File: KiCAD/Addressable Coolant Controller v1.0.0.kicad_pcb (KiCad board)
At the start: 2 copper layers, 117.2 x 159.5 mm, 56 parts, among them J1 XW4M-10D2-H1DS, J2 XW4M-02D1-H1DA, K1 G5V-1, K2 G5V-1, K3 G5V-1, K4 G5V-1, K5 G5V-1, K6 G5V-1, K7 G5V-1, K8 G5V-1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

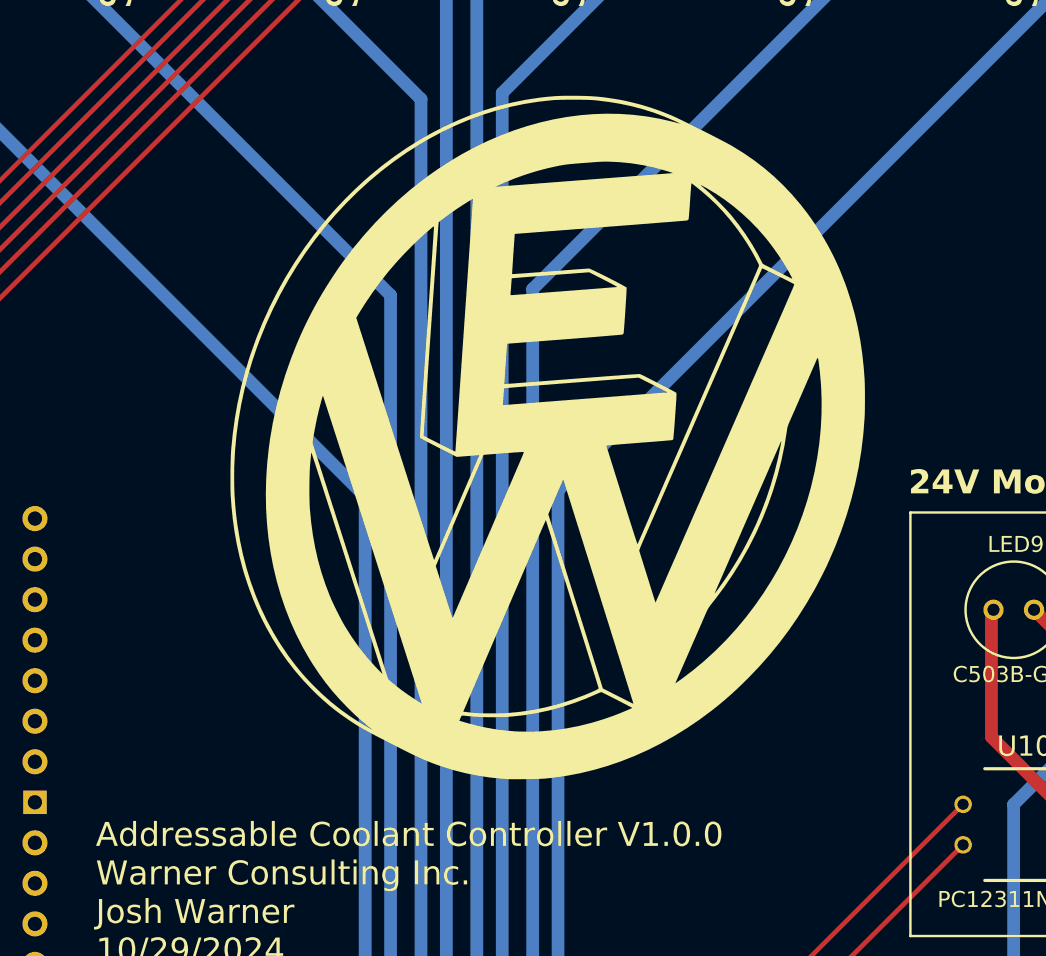
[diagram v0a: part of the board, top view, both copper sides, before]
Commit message: Renamed to Addressable Coolant Controller v1.0.0
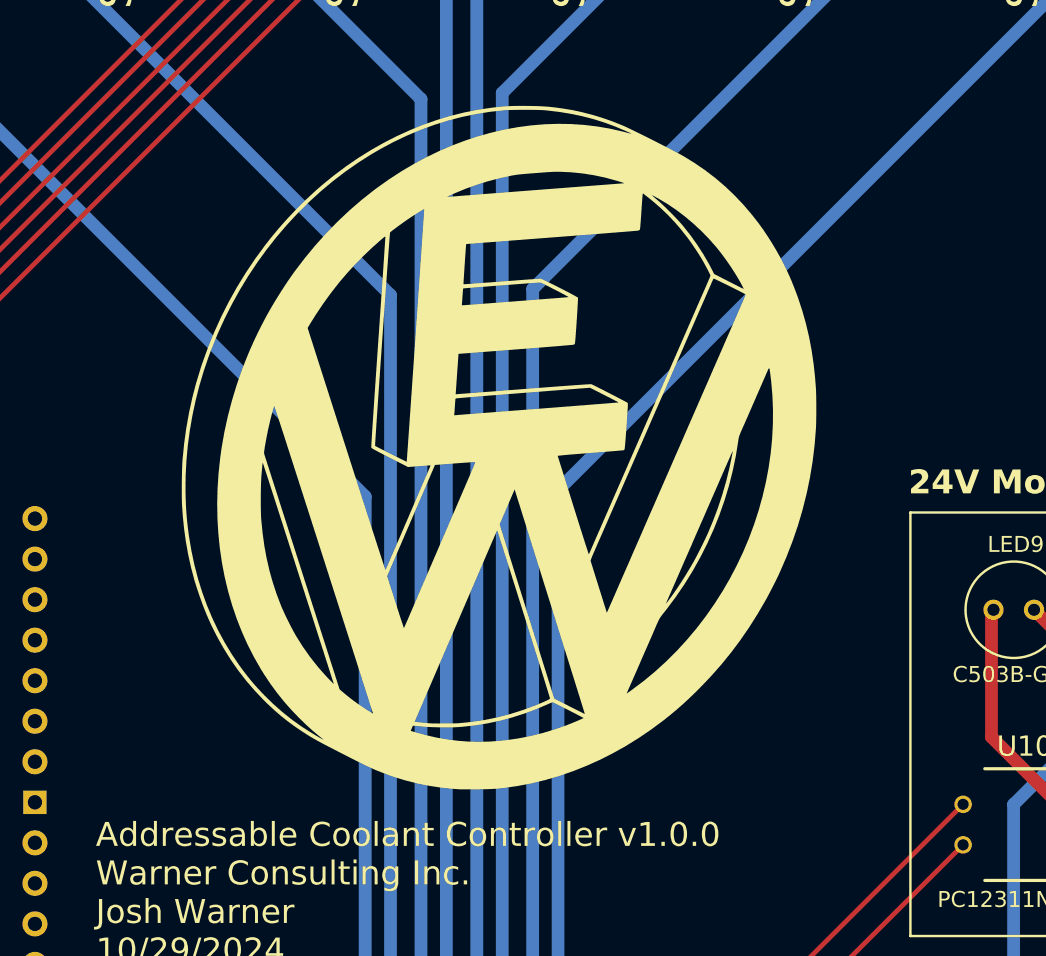
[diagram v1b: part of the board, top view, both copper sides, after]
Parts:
- moved G*** 3.11 mm to (95.9, 133.7)
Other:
- board text added: "Addressable Coolant Controller v1.0.0 Warner Consulting Inc. Josh Warner 10/29/2024"
- board text removed: "Addressable Coolant Controller V1.0.0 Warner Consulting Inc. Josh Warner 10/29/2024"
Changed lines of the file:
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@@
   )
   (footprint "Warner Consulting Logo:Warner Consulting Logo" (layer "F.Cu")
-    (at 98.933 133.096)
+    (at 95.885 133.731)
     (attr board_only exclude_from_pos_files exclude_from_bom)
     (fp_text reference "G***" (at 0 0) (layer "F.SilkS")
@@
     (effects (font (size 2 2) (thickness 0.25)) (justify right))
   )
-  (gr_text "Addressable Coolant Controller V1.0.0\nWarner Consulting Inc.\nJosh Warner\n10/29/2024" (at 70.612 166.116) (layer "F.SilkS")
+  (gr_text "Addressable Coolant Controller v1.0.0\nWarner Consulting Inc.\nJosh Warner\n10/29/2024" (at 70.612 166.116) (layer "F.SilkS")
     (effects (font (size 1.5 1.5) (thickness 0.15)) (justify left bottom))
   )
